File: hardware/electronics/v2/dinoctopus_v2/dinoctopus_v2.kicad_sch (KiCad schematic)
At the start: 3 parts, among them J1 Conn_01x04_Socket, J2 Conn_01x03_Pin, U1 Pico mounting

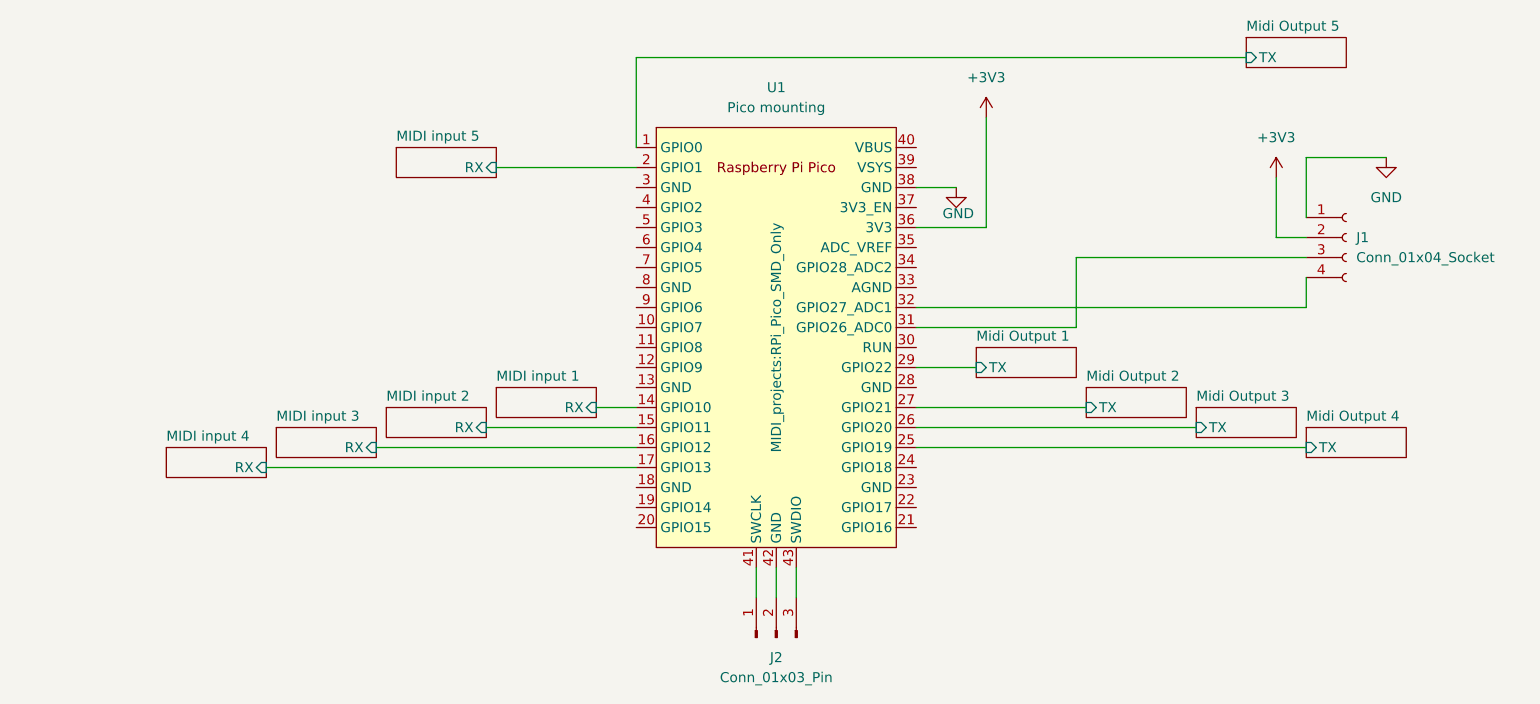
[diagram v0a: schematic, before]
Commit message: Rework schemas with JLCPCB references
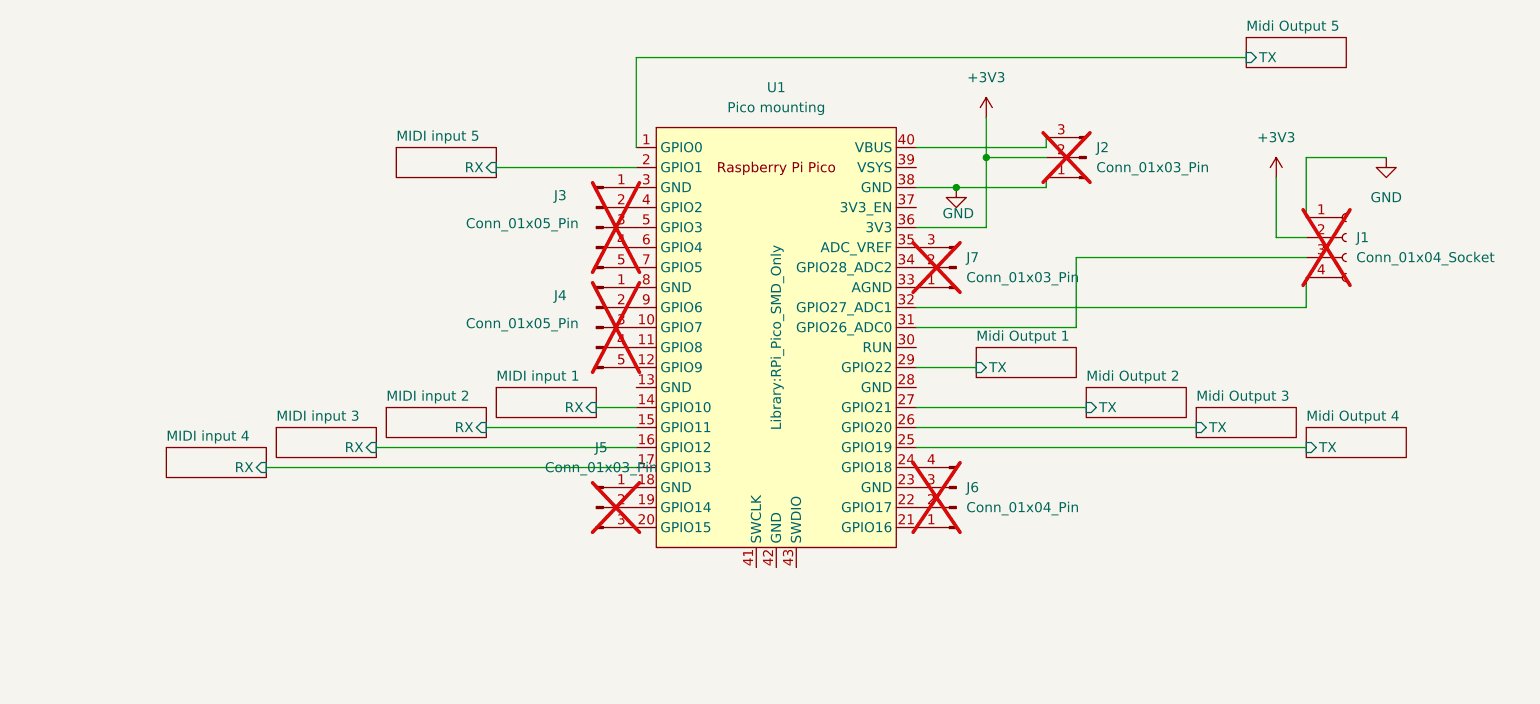
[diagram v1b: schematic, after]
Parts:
- added J3, J4: Conn_01x05_Pin, Connector_PinHeader_2.54mm:PinHeader_1x05_P2.54mm_Vertical, symbol Connector:Conn_01x05_Pin
- added J5, J7: Conn_01x03_Pin, Connector_PinHeader_2.54mm:PinHeader_1x03_P2.54mm_Vertical, symbol Connector:Conn_01x03_Pin
- added J6: Conn_01x04_Pin, Connector_PinHeader_2.54mm:PinHeader_1x04_P2.54mm_Vertical, symbol Connector:Conn_01x04_Pin
- J1: footprint MIDI_projects:JST_SH_SM04B-SRSS-TB_1x04-1MP_P1.00mm_Horizontal -> Library:JST_SH_SM04B-SRSS-TB_1x04-1MP_P1.00mm_Horizontal; now not fitted
- J2: now not fitted
- U1: footprint MIDI_projects:RPi_Pico_SMD_Only -> Library:RPi_Pico_SMD_Only
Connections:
- net +3V3: now also J2.2 (Pin_2)
- net GND: now also J2.1 (Pin_1)
- net at U1.41 (SWCLK): no longer J2.1 (Pin_1)
- net at U1.42 (GND): no longer J2.2 (Pin_2)
- net at J2.3 (Pin_3): now also U1.40 (VBUS); no longer U1.43 (SWDIO)
- net at U1.10 (GPIO7): now also J4.3 (Pin_3)
- net at U1.11 (GPIO8): now also J4.4 (Pin_4)
- net at U1.12 (GPIO9): now also J4.5 (Pin_5)
- net at U1.18 (GND): now also J5.1 (Pin_1)
- net at U1.19 (GPIO14): now also J5.2 (Pin_2)
- net at U1.20 (GPIO15): now also J5.3 (Pin_3)
- net at U1.21 (GPIO16): now also J6.1 (Pin_1)
- net at U1.22 (GPIO17): now also J6.2 (Pin_2)
- net at U1.23 (GND): now also J6.3 (Pin_3)
- net at U1.24 (GPIO18): now also J6.4 (Pin_4)
- net at U1.3 (GND): now also J3.1 (Pin_1)
- net at U1.33 (AGND): now also J7.1 (Pin_1)
- net at U1.34 (GPIO28_ADC2): now also J7.2 (Pin_2)
- net at U1.35 (ADC_VREF): now also J7.3 (Pin_3)
- net at U1.4 (GPIO2): now also J3.2 (Pin_2)
- net at U1.5 (GPIO3): now also J3.3 (Pin_3)
- net at U1.6 (GPIO4): now also J3.4 (Pin_4)
- net at U1.7 (GPIO5): now also J3.5 (Pin_5)
- net at U1.8 (GND): now also J4.1 (Pin_1)
- net at U1.9 (GPIO6): now also J4.2 (Pin_2)

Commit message: giant mess
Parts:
- removed J2, J5, J7: Conn_01x03_Pin, Connector_PinHeader_2.54mm:PinHeader_1x03_P2.54mm_Vertical, symbol Connector:Conn_01x03_Pin
- removed J3, J4: Conn_01x05_Pin, Connector_PinHeader_2.54mm:PinHeader_1x05_P2.54mm_Vertical, symbol Connector:Conn_01x05_Pin
- removed J6: Conn_01x04_Pin, Connector_PinHeader_2.54mm:PinHeader_1x04_P2.54mm_Vertical, symbol Connector:Conn_01x04_Pin
- added J3, J4: Conn_01x20_Pin, Connector_PinSocket_2.54mm:PinSocket_1x20_P2.54mm_Vertical, symbol Connector:Conn_01x20_Pin
- U1: footprint Library:RPi_Pico_SMD_Only -> Library:RPi_Pico_Holes_; now not fitted; now left out of the parts list
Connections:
- net +3V3: now also J4.5 (Pin_5)
- net GND: now also J4.3 (Pin_3)
- net MIDI input 1/RX: now also J3.14 (Pin_14)
- net MIDI input 2/RX: now also J3.15 (Pin_15)
- net MIDI input 3/RX: now also J3.16 (Pin_16)
- net MIDI input 4/RX: now also J3.17 (Pin_17)
- net MIDI input 5/RX: now also J3.2 (Pin_2)
- net Midi Output 1/TX: now also J4.12 (Pin_12)
- net Midi Output 2/TX: now also J4.14 (Pin_14)
- net Midi Output 3/TX: now also J4.15 (Pin_15)
- net Midi Output 4/TX: now also J4.16 (Pin_16)
- net Midi Output 5/TX: now also J3.1 (Pin_1)
- net at U1.8 (GND): now also J3.8 (Pin_8)
- net at U1.9 (GPIO6): now also J3.9 (Pin_9)
- net at U1.10 (GPIO7): now also J3.10 (Pin_10)
- net at U1.11 (GPIO8): now also J3.11 (Pin_11)
- net at U1.12 (GPIO9): now also J3.12 (Pin_12)
- net at U1.21 (GPIO16): now also J4.20 (Pin_20)
- net at U1.22 (GPIO17): now also J4.19 (Pin_19)
- net at U1.23 (GND): now also J4.18 (Pin_18)
- net at U1.24 (GPIO18): now also J4.17 (Pin_17)
- net at J1.3 (Pin_3), U1.31 (GPIO26_ADC0): now also J4.10 (Pin_10)
- net at J1.4 (Pin_4), U1.32 (GPIO27_ADC1): now also J4.9 (Pin_9)
- net at U1.33 (AGND): now also J4.8 (Pin_8)
- net at U1.34 (GPIO28_ADC2): now also J4.7 (Pin_7)
- net at U1.35 (ADC_VREF): now also J4.6 (Pin_6)
- net at U1.40 (VBUS): now also J4.1 (Pin_1)
- net at U1.3 (GND): now also J3.3 (Pin_3)
- net at U1.4 (GPIO2): now also J3.4 (Pin_4)
- net at U1.5 (GPIO3): now also J3.5 (Pin_5)
- net at U1.6 (GPIO4): now also J3.6 (Pin_6)
- net at U1.7 (GPIO5): now also J3.7 (Pin_7)
- net at U1.13 (GND): now also J3.13 (Pin_13)
- net at U1.18 (GND): now also J3.18 (Pin_18)
- net at U1.19 (GPIO14): now also J3.19 (Pin_19)
- net at U1.20 (GPIO15): now also J3.20 (Pin_20)
- net at U1.28 (GND): now also J4.13 (Pin_13)
- net at U1.30 (RUN): now also J4.11 (Pin_11)
- net at U1.37 (3V3_EN): now also J4.4 (Pin_4)
- net at U1.39 (VSYS): now also J4.2 (Pin_2)
